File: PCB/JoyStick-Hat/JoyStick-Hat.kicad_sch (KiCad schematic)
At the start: 0 parts

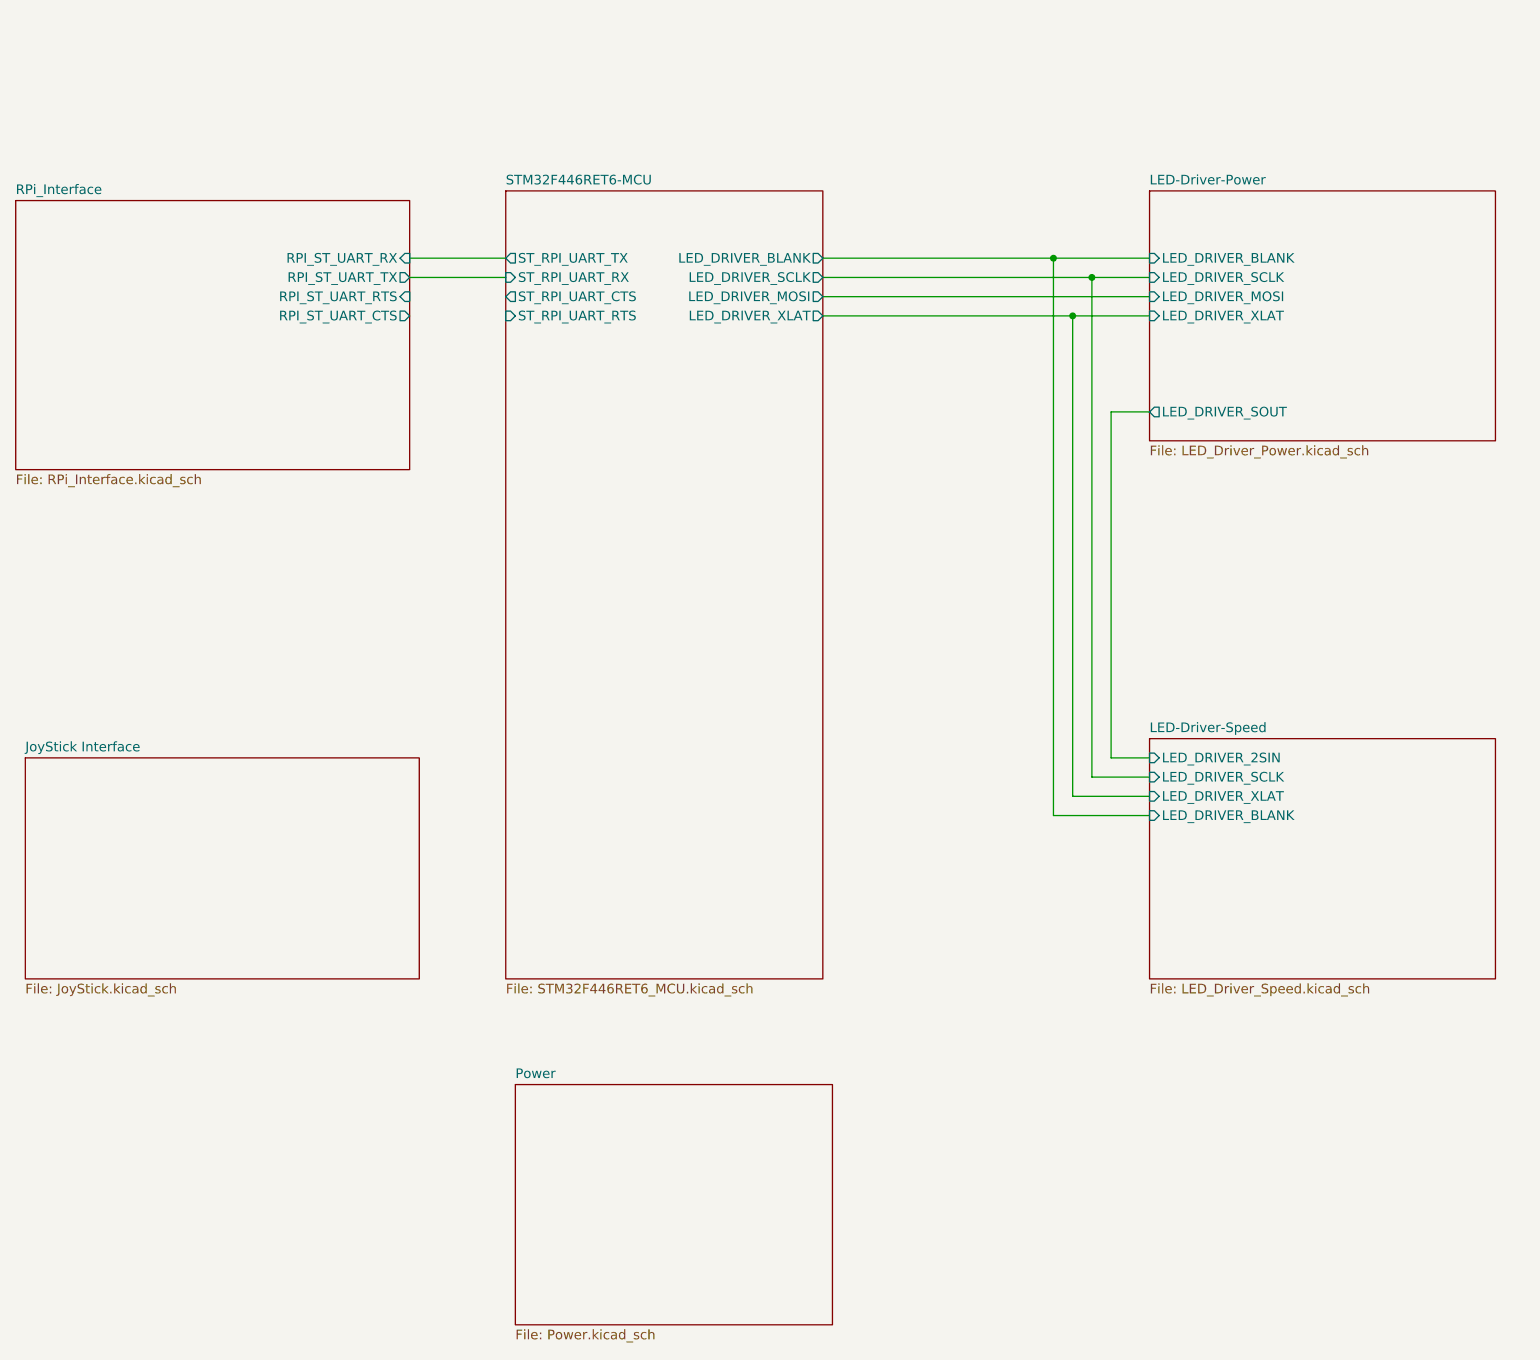
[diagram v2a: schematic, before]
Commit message: Sheet Conenctivity and RS485
Added more sheet entries throughuot the project connecting different subsystems to the main MCU schematic. Also added  new sheet for the RS485 interface for communicating with the motor control board.
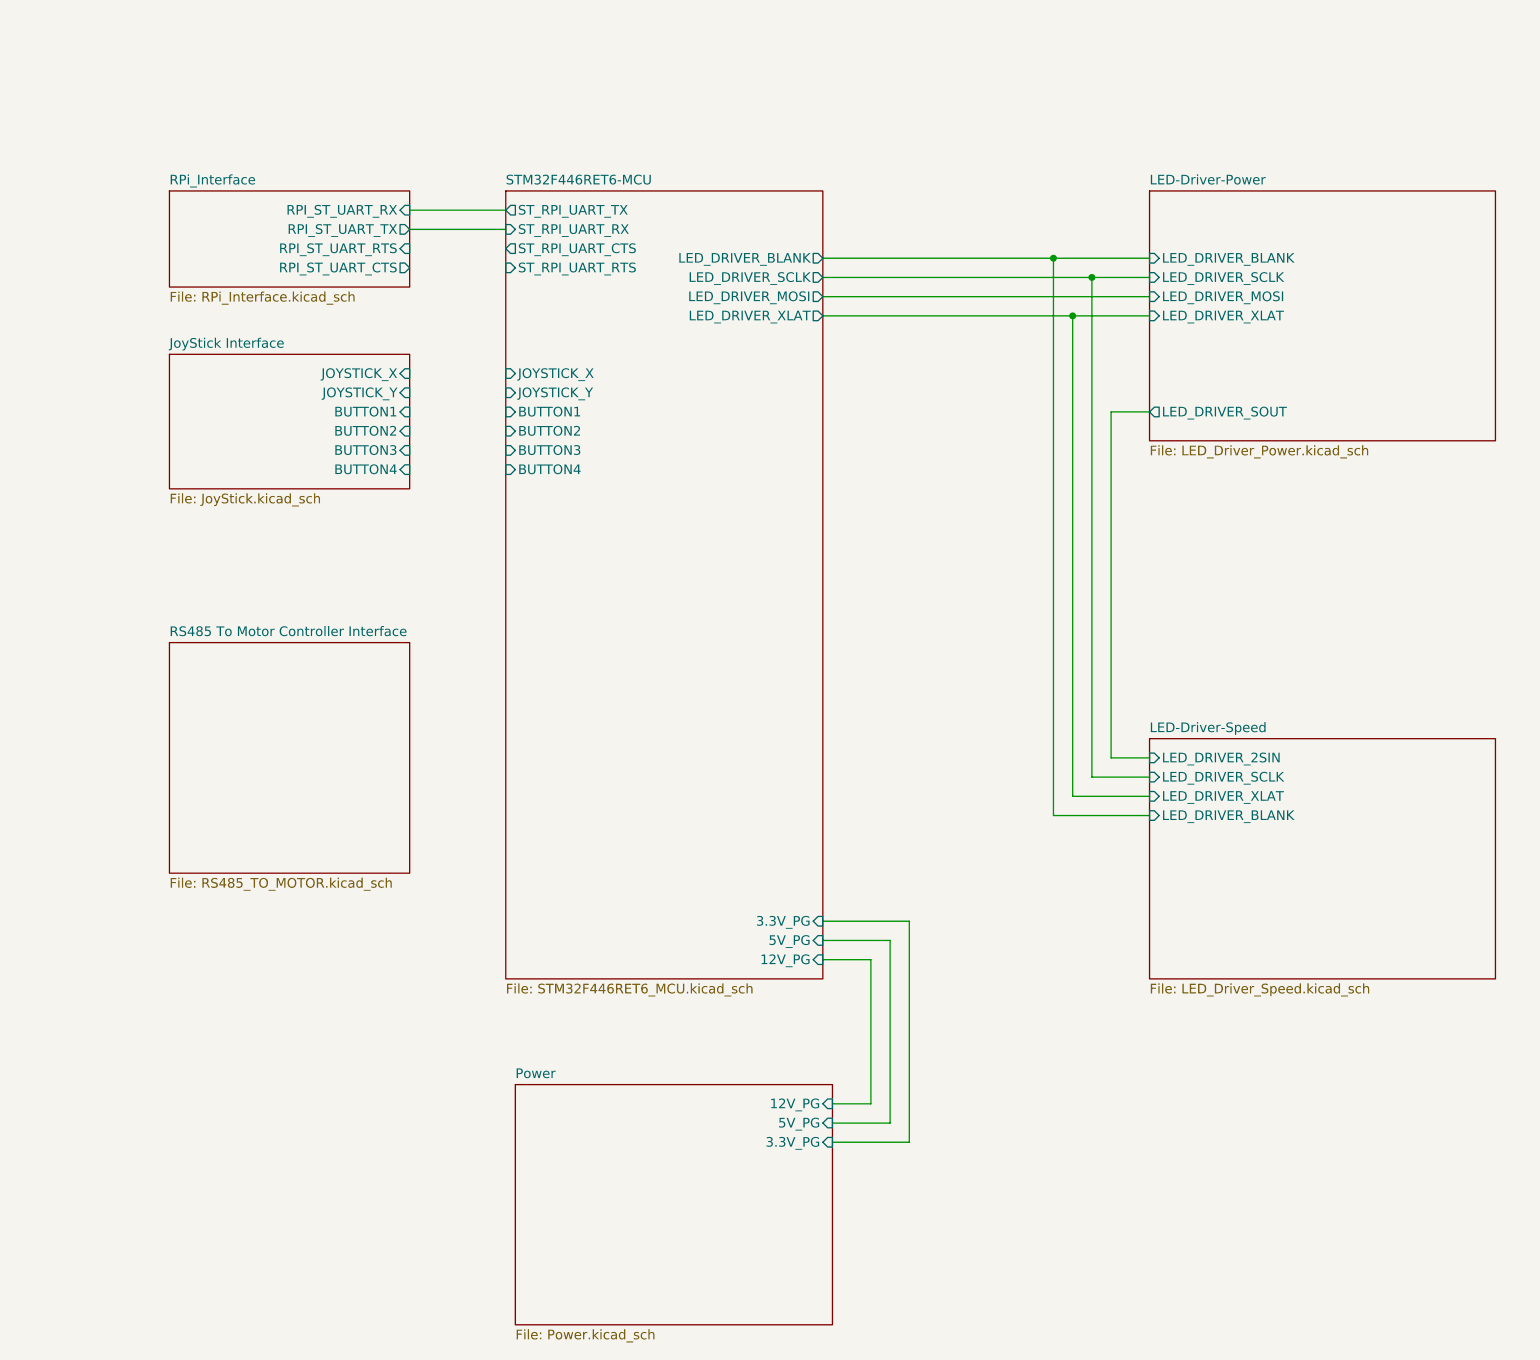
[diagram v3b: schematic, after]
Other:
- added sheet RS485 To Motor Controller Interface (RS485_TO_MOTOR.kicad_sch)
- sheet JoyStick Interface ports: added BUTTON1, BUTTON2, BUTTON3, BUTTON4, JOYSTICK_X, JOYSTICK_Y; removed none
- sheet Power ports: added 12V_PG, 3.3V_PG, 5V_PG; removed none
- sheet STM32F446RET6-MCU ports: added 12V_PG, 3.3V_PG, 5V_PG, BUTTON1, BUTTON2, BUTTON3, BUTTON4, JOYSTICK_X, JOYSTICK_Y; removed none
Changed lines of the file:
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@@
+    (stroke (width 0) (type default))
+  )
+  (wire (pts (xy 166.37 138.43) (xy 154.94 138.43))
     (stroke (width 0) (type default))
   )
@@
     (stroke (width 0) (type default))
   )
-  (wire (pts (xy 100.33 53.34) (xy 113.03 53.34))
+  (wire (pts (xy 100.33 46.99) (xy 113.03 46.99))
+    (stroke (width 0) (type default))
+  )
+  (wire (pts (xy 156.21 165.1) (xy 163.83 165.1))
     (stroke (width 0) (type default))
   )
@@
     (stroke (width 0) (type default))
   )
+  (wire (pts (xy 154.94 140.97) (xy 163.83 140.97))
+    (stroke (width 0) (type default))
+  )
+  (wire (pts (xy 161.29 162.56) (xy 161.29 143.51))
+    (stroke (width 0) (type default))
+  )
+  (wire (pts (xy 161.29 143.51) (xy 154.94 143.51))
+    (stroke (width 0) (type default))
+  )
+  (wire (pts (xy 156.21 167.64) (xy 166.37 167.64))
+    (stroke (width 0) (type default))
+  )
   (wire (pts (xy 193.04 71.12) (xy 198.12 71.12))
     (stroke (width 0) (type default))
@@
     (stroke (width 0) (type default))
   )
+  (wire (pts (xy 166.37 167.64) (xy 166.37 138.43))
+    (stroke (width 0) (type default))
+  )
   (wire (pts (xy 154.94 55.88) (xy 198.12 55.88))
     (stroke (width 0) (type default))
@@
     (stroke (width 0) (type default))
   )
+  (wire (pts (xy 163.83 165.1) (xy 163.83 140.97))
+    (stroke (width 0) (type default))
+  )
+  (wire (pts (xy 156.21 162.56) (xy 161.29 162.56))
+    (stroke (width 0) (type default))
+  )
   (wire (pts (xy 193.04 116.84) (xy 193.04 71.12))
     (stroke (width 0) (type default))
@@
     (stroke (width 0) (type default))
   )
-  (wire (pts (xy 100.33 50.8) (xy 113.03 50.8))
+  (wire (pts (xy 100.33 44.45) (xy 113.03 44.45))
     (stroke (width 0) (type default))
   )
@@
     )
   )
-  (sheet (at 49.53 116.84) (size 52.07 29.21) (fields_autoplaced)
+  (sheet (at 68.58 63.5) (size 31.75 17.78) (fields_autoplaced)
     (stroke (width 0.1524) (type solid))
     (fill (color 255 0 255 1.0000))
-    (property "Sheetname" "JoyStick Interface" (at 49.53 116.1284 0)
-      (effects (font (size 1.27 1.27)) (justify left bottom))
-    )
-    (property "Sheetfile" "JoyStick.kicad_sch" (at 49.53 146.6346 0)
-      (effects (font (size 1.27 1.27)) (justify left top))
+    (property "Sheetname" "JoyStick Interface" (at 68.58 62.7884 0)
+      (effects (font (size 1.27 1.27)) (justify left bottom))
+    )
+    (property "Sheetfile" "JoyStick.kicad_sch" (at 68.58 81.8646 0)
+      (effects (font (size 1.27 1.27)) (justify left top))
+    )
+    (pin "JOYSTICK_X" input (at 100.33 66.04 0)
+      (effects (font (size 1.27 1.27)) (justify right))
+    )
+    (pin "JOYSTICK_Y" input (at 100.33 68.58 0)
+      (effects (font (size 1.27 1.27)) (justify right))
+    )
+    (pin "BUTTON2" input (at 100.33 73.66 0)
+      (effects (font (size 1.27 1.27)) (justify right))
+    )
+    (pin "BUTTON3" input (at 100.33 76.2 0)
+      (effects (font (size 1.27 1.27)) (justify right))
+    )
+    (pin "BUTTON4" input (at 100.33 78.74 0)
+      (effects (font (size 1.27 1.27)) (justify right))
+    )
+    (pin "BUTTON1" input (at 100.33 71.12 0)
+      (effects (font (size 1.27 1.27)) (justify right))
     )
     (instances
@@
     )
   )
-  (sheet (at 48.26 43.18) (size 52.07 35.56) (fields_autoplaced)
+  (sheet (at 68.58 101.6) (size 31.75 30.48) (fields_autoplaced)
+    (stroke (width 0.1524) (type solid))
+    (fill (color 255 153 0 1.0000))
+    (property "Sheetname" "RS485 To Motor Controller Interface" (at 68.58 100.8884 0)
+      (effects (font (size 1.27 1.27)) (justify left bottom))
+    )
+    (property "Sheetfile" "RS485_TO_MOTOR.kicad_sch" (at 68.58 132.6646 0)
+      (effects (font (size 1.27 1.27)) (justify left top))
+    )
+    (instances
+      (project "JoyStick-Hat"
+        (path "/cf0c81b5-5bdf-47c3-83c0-f6980f515e65" (page "8"))
+      )
+    )
+  )
+  (sheet (at 68.58 41.91) (size 31.75 12.7) (fields_autoplaced)
     (stroke (width 0.1524) (type solid))
     (fill (color 0 194 0 1.0000))
-    (property "Sheetname" "RPi_Interface" (at 48.26 42.4684 0)
-      (effects (font (size 1.27 1.27)) (justify left bottom))
-    )
-    (property "Sheetfile" "RPi_Interface.kicad_sch" (at 48.26 79.3246 0)
-      (effects (font (size 1.27 1.27)) (justify left top))
-    )
-    (pin "RPI_ST_UART_RX" input (at 100.33 50.8 0)
-      (effects (font (size 1.27 1.27)) (justify right))
-    )
-    (pin "RPI_ST_UART_TX" output (at 100.33 53.34 0)
-      (effects (font (size 1.27 1.27)) (justify right))
-    )
-    (pin "RPI_ST_UART_RTS" input (at 100.33 55.88 0)
-      (effects (font (size 1.27 1.27)) (justify right))
-    )
-    (pin "RPI_ST_UART_CTS" output (at 100.33 58.42 0)
+    (property "Sheetname" "RPi_Interface" (at 68.58 41.1984 0)
+      (effects (font (size 1.27 1.27)) (justify left bottom))
+    )
+    (property "Sheetfile" "RPi_Interface.kicad_sch" (at 68.58 55.1946 0)
+      (effects (font (size 1.27 1.27)) (justify left top))
+    )
+    (pin "RPI_ST_UART_RX" input (at 100.33 44.45 0)
+      (effects (font (size 1.27 1.27)) (justify right))
+    )
+    (pin "RPI_ST_UART_TX" output (at 100.33 46.99 0)
+      (effects (font (size 1.27 1.27)) (justify right))
+    )
+    (pin "RPI_ST_UART_RTS" input (at 100.33 49.53 0)
+      (effects (font (size 1.27 1.27)) (justify right))
+    )
+    (pin "RPI_ST_UART_CTS" output (at 100.33 52.07 0)
       (effects (font (size 1.27 1.27)) (justify right))
     )
@@
       (effects (font (size 1.27 1.27)) (justify left top))
     )
+    (pin "12V_PG" input (at 156.21 162.56 0)
+      (effects (font (size 1.27 1.27)) (justify right))
+    )
+    (pin "5V_PG" input (at 156.21 165.1 0)
+      (effects (font (size 1.27 1.27)) (justify right))
+    )
+    (pin "3.3V_PG" input (at 156.21 167.64 0)
+      (effects (font (size 1.27 1.27)) (justify right))
+    )
     (instances
       (project "JoyStick-Hat"
@@
       (effects (font (size 1.27 1.27)) (justify left top))
     )
-    (pin "ST_RPI_UART_CTS" output (at 113.03 55.88 180)
-      (effects (font (size 1.27 1.27)) (justify left))
-    )
-    (pin "ST_RPI_UART_RX" input (at 113.03 53.34 180)
-      (effects (font (size 1.27 1.27)) (justify left))
-    )
-    (pin "ST_RPI_UART_TX" output (at 113.03 50.8 180)
-      (effects (font (size 1.27 1.27)) (justify left))
-    )
-    (pin "ST_RPI_UART_RTS" input (at 113.03 58.42 180)
+    (pin "ST_RPI_UART_CTS" output (at 113.03 49.53 180)
+      (effects (font (size 1.27 1.27)) (justify left))
+    )
+    (pin "ST_RPI_UART_RX" input (at 113.03 46.99 180)
+      (effects (font (size 1.27 1.27)) (justify left))
+    )
+    (pin "ST_RPI_UART_TX" output (at 113.03 44.45 180)
+      (effects (font (size 1.27 1.27)) (justify left))
+    )
+    (pin "ST_RPI_UART_RTS" input (at 113.03 52.07 180)
       (effects (font (size 1.27 1.27)) (justify left))
     )
@@
       (effects (font (size 1.27 1.27)) (justify right))
     )
+    (pin "BUTTON1" input (at 113.03 71.12 180)
+      (effects (font (size 1.27 1.27)) (justify left))
+    )
+    (pin "BUTTON3" input (at 113.03 76.2 180)
+      (effects (font (size 1.27 1.27)) (justify left))
+    )
+    (pin "BUTTON2" input (at 113.03 73.66 180)
+      (effects (font (size 1.27 1.27)) (justify left))
+    )
+    (pin "BUTTON4" input (at 113.03 78.74 180)
+      (effects (font (size 1.27 1.27)) (justify left))
+    )
+    (pin "JOYSTICK_X" input (at 113.03 66.04 180)
+      (effects (font (size 1.27 1.27)) (justify left))
+    )
+    (pin "JOYSTICK_Y" input (at 113.03 68.58 180)
+      (effects (font (size 1.27 1.27)) (justify left))
+    )
+    (pin "12V_PG" input (at 154.94 143.51 0)
+      (effects (font (size 1.27 1.27)) (justify right))
+    )
+    (pin "3.3V_PG" input (at 154.94 138.43 0)
+      (effects (font (size 1.27 1.27)) (justify right))
+    )
+    (pin "5V_PG" input (at 154.94 140.97 0)
+      (effects (font (size 1.27 1.27)) (justify right))
+    )

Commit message: Schematic Progress
Made progress with schematic and corrected designator letters with connectors to match the built in paradigm of using J instead of T. T will not be used to referencing transformers instead of connectors.
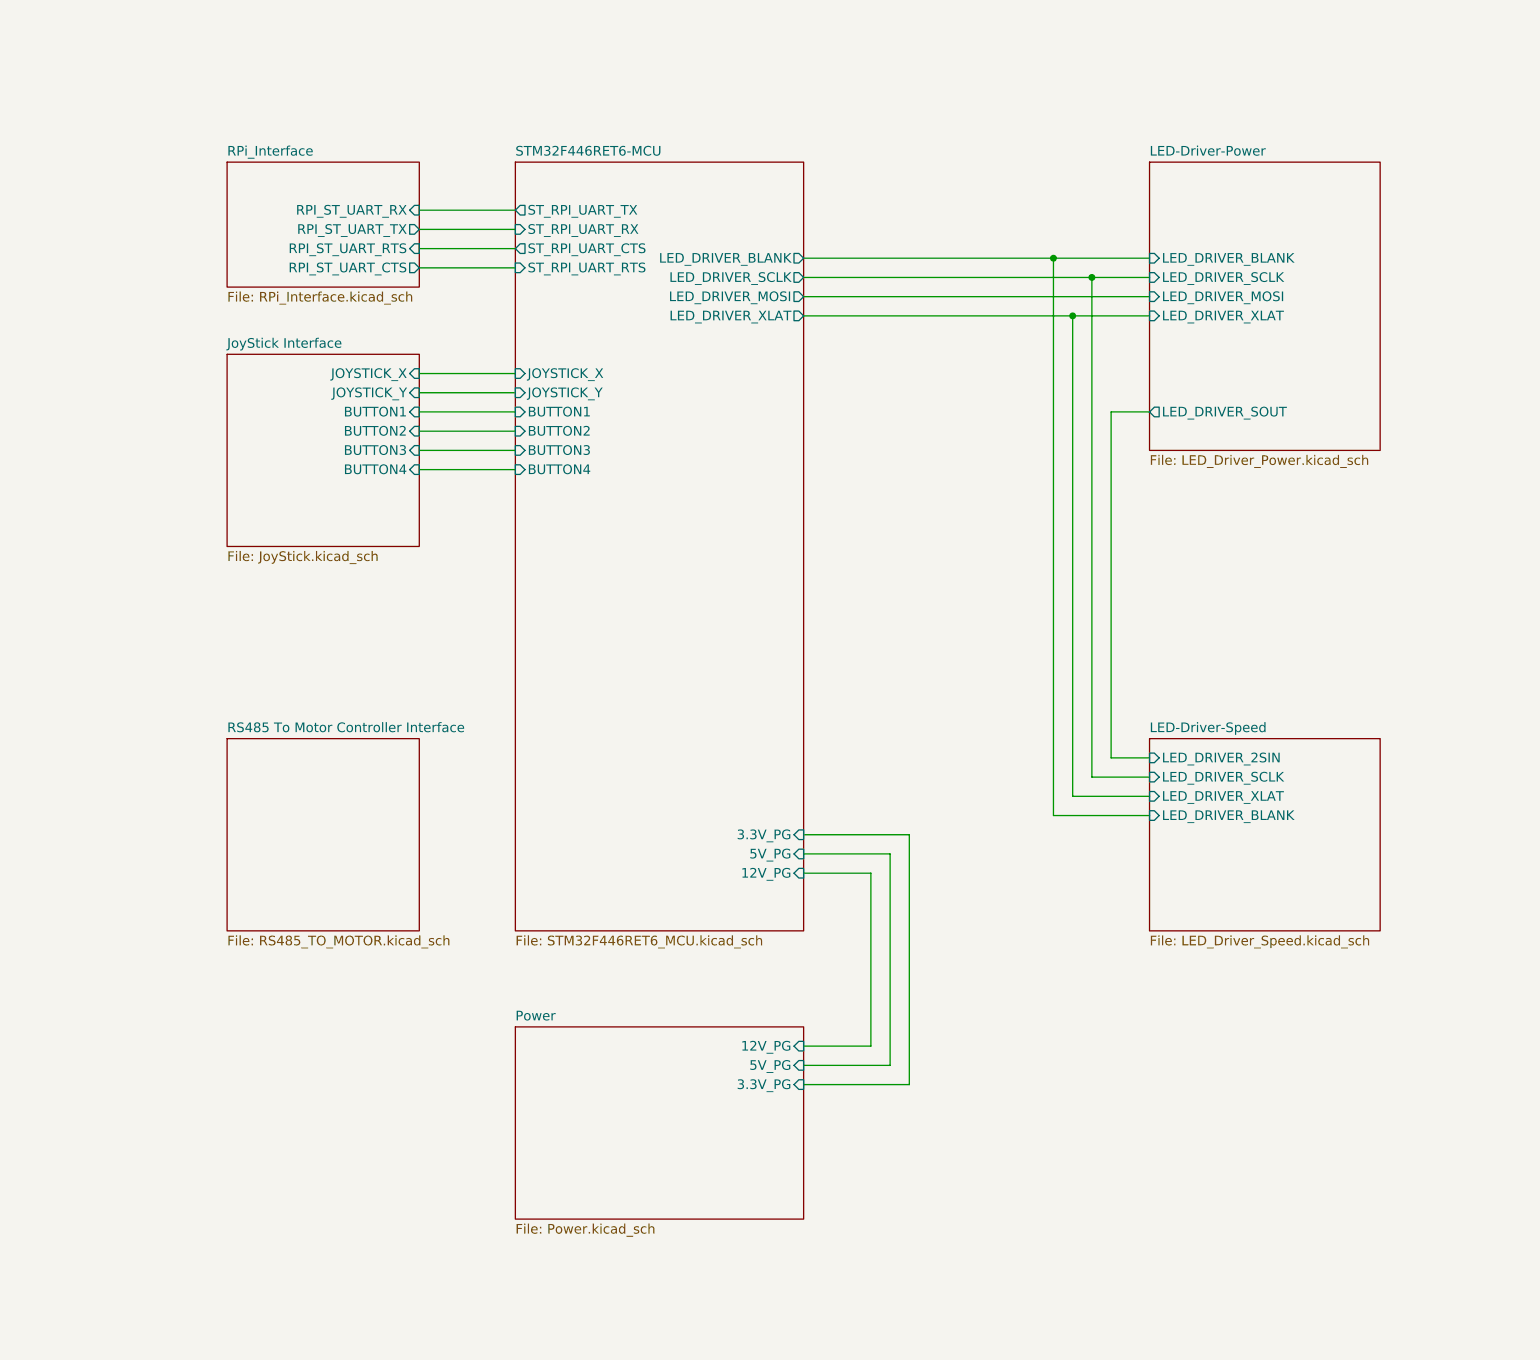
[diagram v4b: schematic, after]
